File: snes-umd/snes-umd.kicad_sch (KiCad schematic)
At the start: 4 parts, among them CON101 UMDv3-CONN, CON102 SNES-CONN, U101 MCP23008T-E_SS

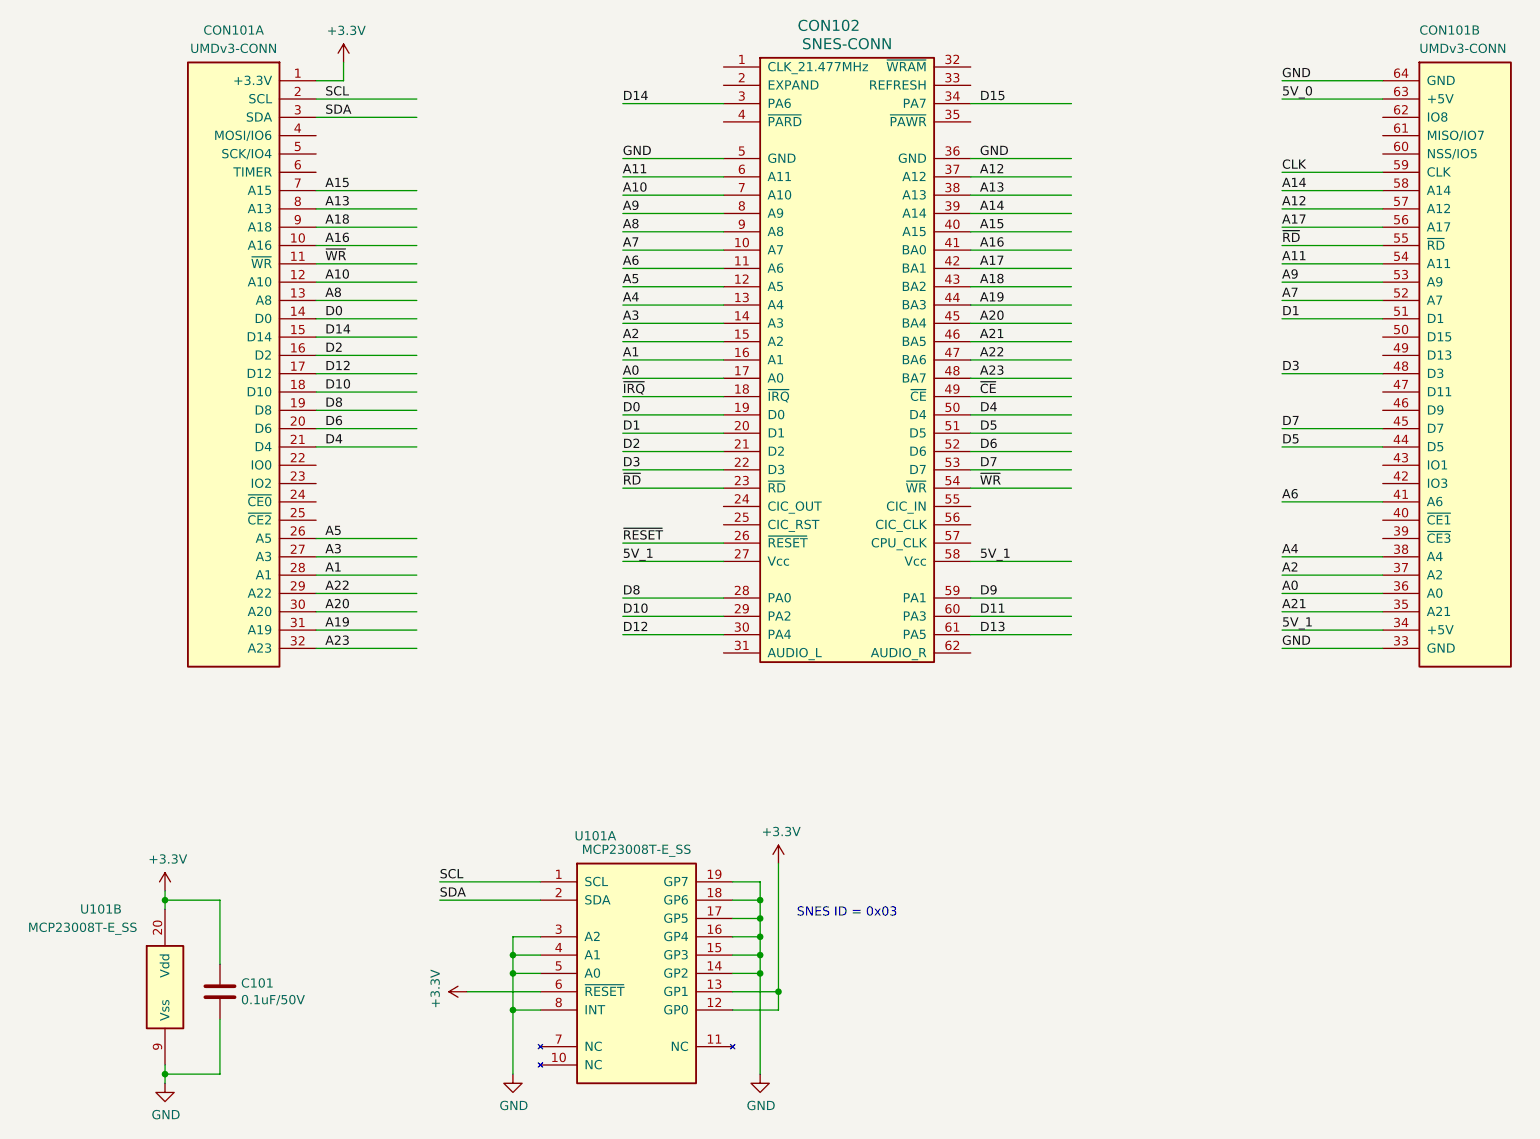
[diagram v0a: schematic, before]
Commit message: board outline and sch mostly done
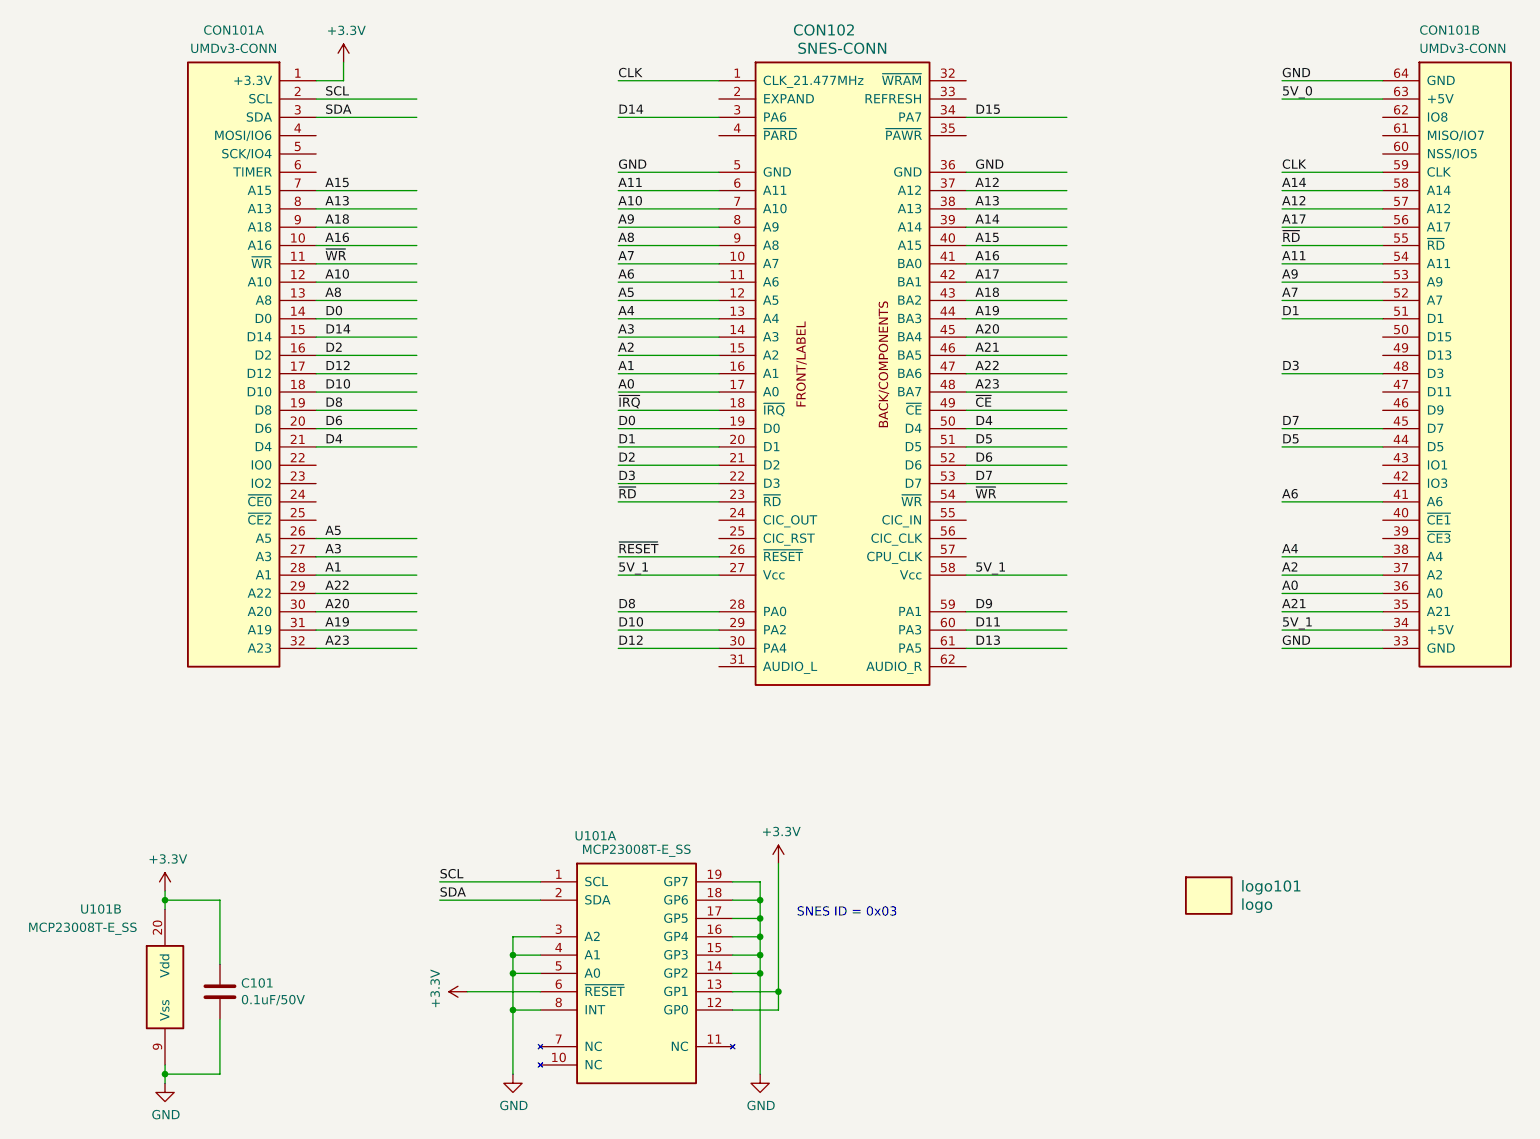
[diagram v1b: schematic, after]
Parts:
- added logo101: logo, db-artwork:db-logo_7.5mm, symbol db-artwork:logo
- CON102: footprint (none) -> db-thparts:SNES-CONN-EXP
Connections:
- net CLK: now also CON102.1 (CLK_21.477MHz)

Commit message: layout almost complete
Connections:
- net D11: now also CON101.47 (D11)
- net D13: now also CON101.49 (D13)
- net D15: now also CON101.50 (D15)
- net D9: now also CON101.46 (D9)
- net ~{CE}: now also CON101.24 (~{CE0})
- net EXPAND: now reaches CON102.2 (EXPAND)
- net EXPAND: now also CON101.4 (MOSI/IO6)
- net ~{WRAM}: now reaches CON102.32 (~{WRAM})
- net ~{WRAM}: now also CON101.62 (IO8)
- net REFRESH: now reaches CON102.33 (REFRESH)
- net REFRESH: now also CON101.61 (MISO/IO7)
- net ~{PAWR}: now reaches CON102.35 (~{PAWR})
- net ~{PAWR}: now also CON101.60 (NSS/IO5)
- net ~{PARD}: now reaches CON102.4 (~{PARD})
- net ~{PARD}: now also CON101.5 (SCK/IO4)
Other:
- moved on the sheet: CON101B
